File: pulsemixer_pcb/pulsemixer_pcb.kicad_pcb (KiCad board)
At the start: 2 copper layers, 69 parts, among them SW101 SW_PG_RIGHT, SW102 SW_PG_LEFT, SW103 SW_STRM_DEV, SW201 Vol_Encoder, SW202 SW_MUTE, SW301 Vol_Encoder, SW302 SW_MUTE, SW401 Vol_Encoder, SW402 SW_MUTE, SW501 Vol_Encoder, SW502 SW_MUTE, U201 MCP23017_SP, U301 MCP23017_SP, U401 MCP23017_SP, U501 MCP23017_SP

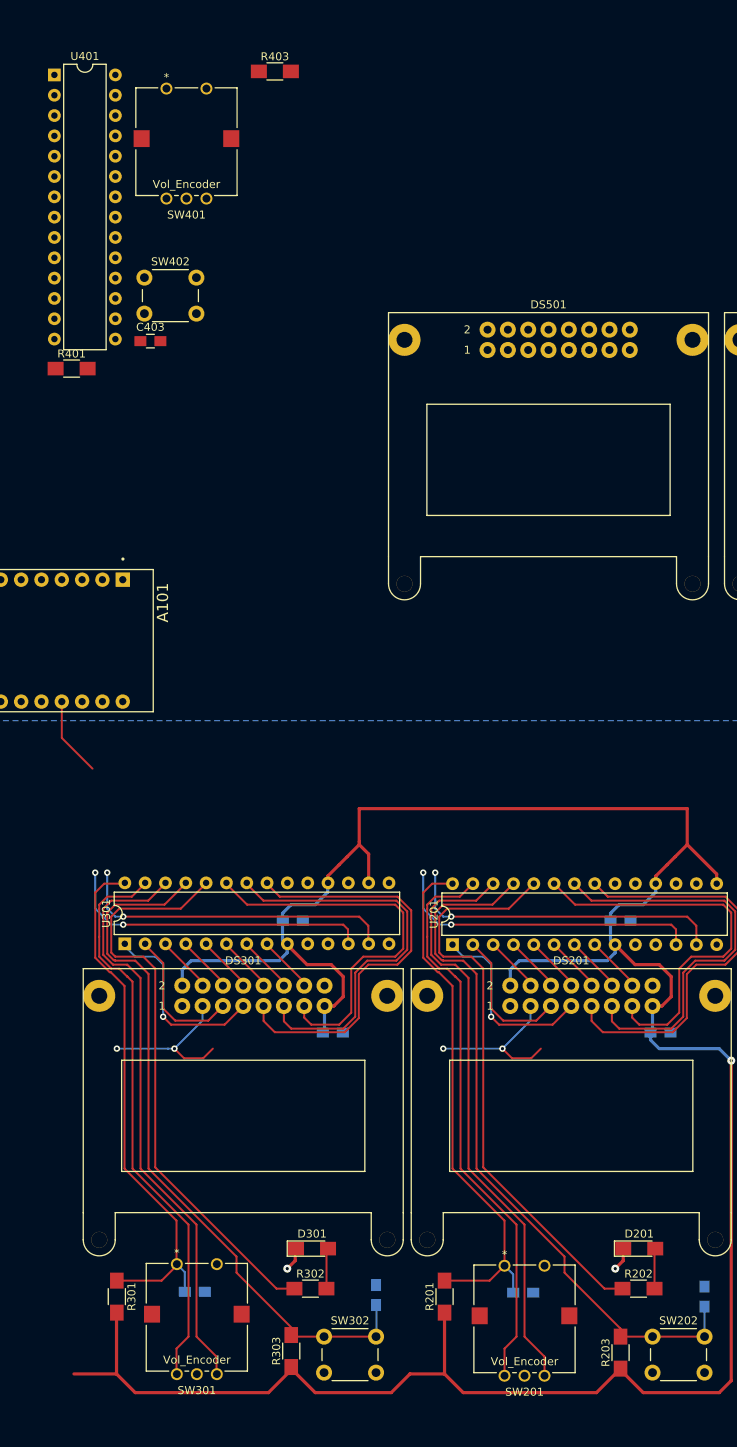
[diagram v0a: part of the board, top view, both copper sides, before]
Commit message: Revised schematic after testing rotary encoder.
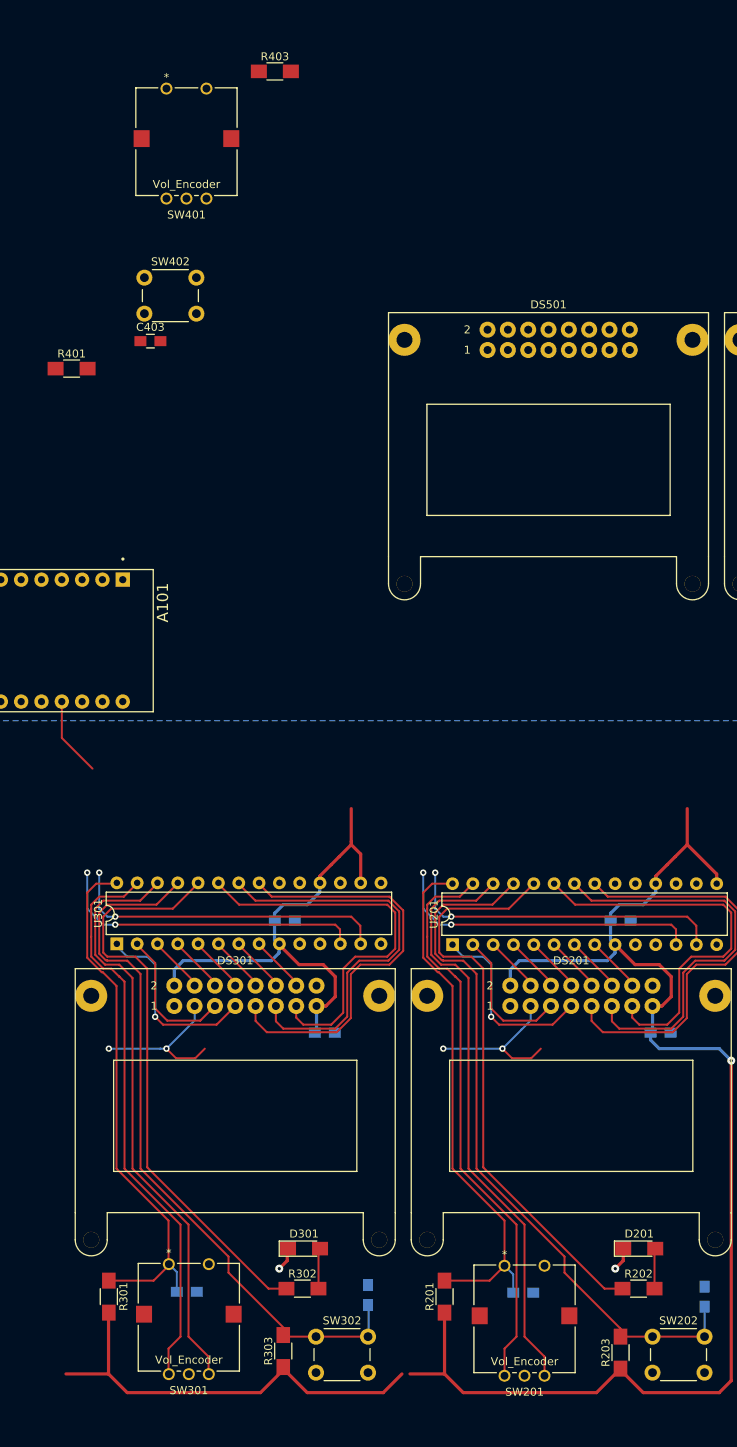
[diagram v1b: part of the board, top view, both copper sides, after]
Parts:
- removed U401: MCP23017_SP, Housings_DIP:DIP-28_W7.62mm
- moved C301 1.00 mm to (144.6, 93.8)
- moved C302 1.00 mm to (122.0, 93.4)
- moved C303 1.00 mm to (134.2, 47.0)
- moved C304 1.00 mm to (139.2, 61.0)
- moved D301 1.00 mm to (136.6, 88.0)
- moved DS301 1.00 mm to (128.0, 53.0)
- moved R301 1.00 mm to (112.2, 94.0)
- moved R302 1.00 mm to (136.4, 93.0)
- moved R303 1.00 mm to (134.0, 100.8)
- moved SW301 1.00 mm to (122.2, 110.8)
- moved SW302 1.00 mm to (138.1, 99.0)
- moved U301 1.00 mm to (113.2, 49.9)
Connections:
- net /sheet5F077D1F/LCD_DB0 renamed /Channel2/LCD_DB0
- net /sheet5F077D1F/LCD_DB1 renamed /Channel2/LCD_DB1
- net /sheet5F077D1F/LCD_DB2 renamed /Channel2/LCD_DB2
- net /sheet5F077D1F/LCD_DB3 renamed /Channel2/LCD_DB3
- net /sheet5F077D1F/LCD_DB4 renamed /Channel2/LCD_DB4
- net /sheet5F077D1F/LCD_DB5 renamed /Channel2/LCD_DB5
- net /sheet5F077D1F/LCD_DB6 renamed /Channel2/LCD_DB6
- net /sheet5F077D1F/LCD_DB7 renamed /Channel2/LCD_DB7
- net /sheet5F077D1F/LCD_E renamed /Channel2/LCD_E
- net /sheet5F077D1F/LCD_RS renamed /Channel2/LCD_RS
- net /sheet5F077D1F/LCD_RW renamed /Channel2/LCD_RW
- net /sheet5F077D1F/MUTE_LED renamed /Channel2/MUTE_LED
- net /sheet5F077D1F/MUTE_SW renamed /Channel2/MUTE_SW
- net /sheet5F077D1F/VOL_A renamed /Channel2/VOL_A
- net /sheet5F077D1F/VOL_B renamed /Channel2/VOL_B
- net /sheet5F077D1F/VOL_SW renamed /Channel2/VOL_SW
- net /sheet5F077D20/MUTE_SW renamed /Channel3/MUTE_SW
- net /sheet5F077D20/VOL_SW renamed /Channel3/VOL_SW
- C201 pad 2: /sheet5F071274/MUTE_SW -> /Channel1/MUTE_SW
- C202 pad 2: /sheet5F071274/VOL_SW -> /Channel1/VOL_SW
- C501 pad 2: /Channel1/MUTE_SW -> /Channel0/MUTE_SW
- C502 pad 2: /Channel1/VOL_SW -> /Channel0/VOL_SW
- DS201 pad 10: /sheet5F071274/LCD_DB3 -> /Channel1/LCD_DB3
- DS201 pad 11: /sheet5F071274/LCD_DB4 -> /Channel1/LCD_DB4
- DS201 pad 12: /sheet5F071274/LCD_DB5 -> /Channel1/LCD_DB5
- DS201 pad 13: /sheet5F071274/LCD_DB6 -> /Channel1/LCD_DB6
- DS201 pad 14: /sheet5F071274/LCD_DB7 -> /Channel1/LCD_DB7
- DS201 pad 4: /sheet5F071274/LCD_RS -> /Channel1/LCD_RS
- DS201 pad 5: /sheet5F071274/LCD_RW -> /Channel1/LCD_RW
- DS201 pad 6: /sheet5F071274/LCD_E -> /Channel1/LCD_E
- DS201 pad 7: /sheet5F071274/LCD_DB0 -> /Channel1/LCD_DB0
- DS201 pad 8: /sheet5F071274/LCD_DB1 -> /Channel1/LCD_DB1
- DS201 pad 9: /sheet5F071274/LCD_DB2 -> /Channel1/LCD_DB2
- DS401 pad 10: /sheet5F077D20/LCD_DB3 -> /Channel3/LCD_DB3
- DS401 pad 11: /sheet5F077D20/LCD_DB4 -> /Channel3/LCD_DB4
- DS401 pad 12: /sheet5F077D20/LCD_DB5 -> /Channel3/LCD_DB5
- DS401 pad 13: /sheet5F077D20/LCD_DB6 -> /Channel3/LCD_DB6
- DS401 pad 14: /sheet5F077D20/LCD_DB7 -> /Channel3/LCD_DB7
- DS401 pad 4: /sheet5F077D20/LCD_RS -> /Channel3/LCD_RS
- DS401 pad 5: /sheet5F077D20/LCD_RW -> /Channel3/LCD_RW
- DS401 pad 6: /sheet5F077D20/LCD_E -> /Channel3/LCD_E
- DS401 pad 7: /sheet5F077D20/LCD_DB0 -> /Channel3/LCD_DB0
- DS401 pad 8: /sheet5F077D20/LCD_DB1 -> /Channel3/LCD_DB1
- DS401 pad 9: /sheet5F077D20/LCD_DB2 -> /Channel3/LCD_DB2
- DS501 pad 10: /Channel1/LCD_DB3 -> /Channel0/LCD_DB3
- DS501 pad 11: /Channel1/LCD_DB4 -> /Channel0/LCD_DB4
- DS501 pad 12: /Channel1/LCD_DB5 -> /Channel0/LCD_DB5
- DS501 pad 13: /Channel1/LCD_DB6 -> /Channel0/LCD_DB6
- DS501 pad 14: /Channel1/LCD_DB7 -> /Channel0/LCD_DB7
- DS501 pad 4: /Channel1/LCD_RS -> /Channel0/LCD_RS
- DS501 pad 5: /Channel1/LCD_RW -> /Channel0/LCD_RW
- DS501 pad 6: /Channel1/LCD_E -> /Channel0/LCD_E
- DS501 pad 7: /Channel1/LCD_DB0 -> /Channel0/LCD_DB0
- DS501 pad 8: /Channel1/LCD_DB1 -> /Channel0/LCD_DB1
- DS501 pad 9: /Channel1/LCD_DB2 -> /Channel0/LCD_DB2
- R201 pad 2: /sheet5F071274/VOL_SW -> /Channel1/VOL_SW
- R202 pad 1: /sheet5F071274/MUTE_LED -> /Channel1/MUTE_LED
- R203 pad 2: /sheet5F071274/MUTE_SW -> /Channel1/MUTE_SW
- R402 pad 1: /sheet5F077D20/MUTE_LED -> /Channel3/MUTE_LED
- R501 pad 2: /Channel1/VOL_SW -> /Channel0/VOL_SW
- R502 pad 1: /Channel1/MUTE_LED -> /Channel0/MUTE_LED
- R503 pad 2: /Channel1/MUTE_SW -> /Channel0/MUTE_SW
- SW201 pad A: /sheet5F071274/VOL_A -> /Channel1/VOL_A
- SW201 pad B: /sheet5F071274/VOL_B -> /Channel1/VOL_B
- SW201 pad S1: /sheet5F071274/VOL_SW -> /Channel1/VOL_SW
- SW202 pad 1: /sheet5F071274/MUTE_SW -> /Channel1/MUTE_SW
- SW401 pad A: /sheet5F077D20/VOL_A -> /Channel3/VOL_A
- SW401 pad B: /sheet5F077D20/VOL_B -> /Channel3/VOL_B
- SW501 pad A: /Channel1/VOL_A -> /Channel0/VOL_A
- SW501 pad B: /Channel1/VOL_B -> /Channel0/VOL_B
- SW501 pad S1: /Channel1/VOL_SW -> /Channel0/VOL_SW
- SW502 pad 1: /Channel1/MUTE_SW -> /Channel0/MUTE_SW
- U201 pad 1: /sheet5F071274/LCD_DB0 -> /Channel1/LCD_DB0
- U201 pad 11: Net-(U201-Pad11) -> (no net)
- U201 pad 14: Net-(U201-Pad14) -> (no net)
- U201 pad 19: /sheet5F071274/INTB -> (no net)
- U201 pad 2: /sheet5F071274/LCD_RW -> /Channel1/LCD_RW
- U201 pad 20: /sheet5F071274/INTA -> (no net)
- U201 pad 21: /sheet5F071274/LCD_DB2 -> /Channel1/LCD_DB2
- U201 pad 22: /sheet5F071274/LCD_DB4 -> /Channel1/LCD_DB4
- U201 pad 23: /sheet5F071274/LCD_DB6 -> /Channel1/LCD_DB6
- U201 pad 24: /sheet5F071274/MUTE_LED -> /Channel1/MUTE_LED
- U201 pad 25: /sheet5F071274/MUTE_SW -> /Channel1/MUTE_SW
- U201 pad 26: /sheet5F071274/VOL_B -> /Channel1/VOL_B
- U201 pad 27: /sheet5F071274/VOL_A -> /Channel1/VOL_A
- U201 pad 28: /sheet5F071274/VOL_SW -> /Channel1/VOL_SW
- U201 pad 3: /sheet5F071274/LCD_RS -> /Channel1/LCD_RS
- U201 pad 4: /sheet5F071274/LCD_E -> /Channel1/LCD_E
- U201 pad 5: /sheet5F071274/LCD_DB1 -> /Channel1/LCD_DB1
- U201 pad 6: /sheet5F071274/LCD_DB3 -> /Channel1/LCD_DB3
- U201 pad 7: /sheet5F071274/LCD_DB5 -> /Channel1/LCD_DB5
- U201 pad 8: /sheet5F071274/LCD_DB7 -> /Channel1/LCD_DB7
- U301 pad 11: (no net) -> Net-(U301-Pad11)
- U301 pad 14: (no net) -> Net-(U301-Pad14)
- U301 pad 19: (no net) -> /Channel2/INTB
- U301 pad 20: (no net) -> /Channel2/INTA
- U501 pad 1: /Channel1/LCD_DB0 -> /Channel0/LCD_DB0
- U501 pad 2: /Channel1/LCD_RW -> /Channel0/LCD_RW
- U501 pad 21: /Channel1/LCD_DB2 -> /Channel0/LCD_DB2
- U501 pad 22: /Channel1/LCD_DB4 -> /Channel0/LCD_DB4
- U501 pad 23: /Channel1/LCD_DB6 -> /Channel0/LCD_DB6
- U501 pad 24: /Channel1/MUTE_LED -> /Channel0/MUTE_LED
- U501 pad 25: /Channel1/MUTE_SW -> /Channel0/MUTE_SW
- U501 pad 26: /Channel1/VOL_B -> /Channel0/VOL_B
- U501 pad 27: /Channel1/VOL_A -> /Channel0/VOL_A
- U501 pad 28: /Channel1/VOL_SW -> /Channel0/VOL_SW
- U501 pad 3: /Channel1/LCD_RS -> /Channel0/LCD_RS
- U501 pad 4: /Channel1/LCD_E -> /Channel0/LCD_E
- U501 pad 5: /Channel1/LCD_DB1 -> /Channel0/LCD_DB1
- U501 pad 6: /Channel1/LCD_DB3 -> /Channel0/LCD_DB3
- U501 pad 7: /Channel1/LCD_DB5 -> /Channel0/LCD_DB5
- U501 pad 8: /Channel1/LCD_DB7 -> /Channel0/LCD_DB7
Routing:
- net /sheet5F071274/MUTE_SW: track 89.7 -> 0.00 mm
- net /Channel1/MUTE_SW: track 0.00 -> 89.7 mm
- net /sheet5F071274/VOL_B: track 74.3 -> 0.00 mm
- net /Channel1/VOL_B: track 0.00 -> 74.3 mm
- net /sheet5F071274/MUTE_LED: track 72.9 -> 0.00 mm
- net /Channel1/MUTE_LED: track 0.00 -> 72.9 mm
- net /sheet5F071274/VOL_A: track 71.5 -> 0.00 mm
- net /Channel1/VOL_A: track 0.00 -> 71.5 mm
- net /sheet5F077D1F/VOL_SW: track 0.00 -> 67.2 mm
- net /Channel2/VOL_SW: track 67.2 -> 0.00 mm
- net /sheet5F071274/VOL_SW: track 67.1 -> 0.00 mm
- net /Channel1/VOL_SW: track 0.00 -> 67.1 mm
- net /sheet5F071274/LCD_DB2: track 52.8 -> 0.00 mm
- net /Channel1/LCD_DB2: track 0.00 -> 52.8 mm
- net /sheet5F071274/LCD_DB4: track 51.3 -> 0.00 mm
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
